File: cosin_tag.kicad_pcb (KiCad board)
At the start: 2 copper layers, 81 x 34 mm, 65 parts, among them IC1 ATTINY13-SS, P1 ISP, Q1 2N7002, Q2 2N7002, Q3 2N7002, Q4 2N7002, Q5 2N7002

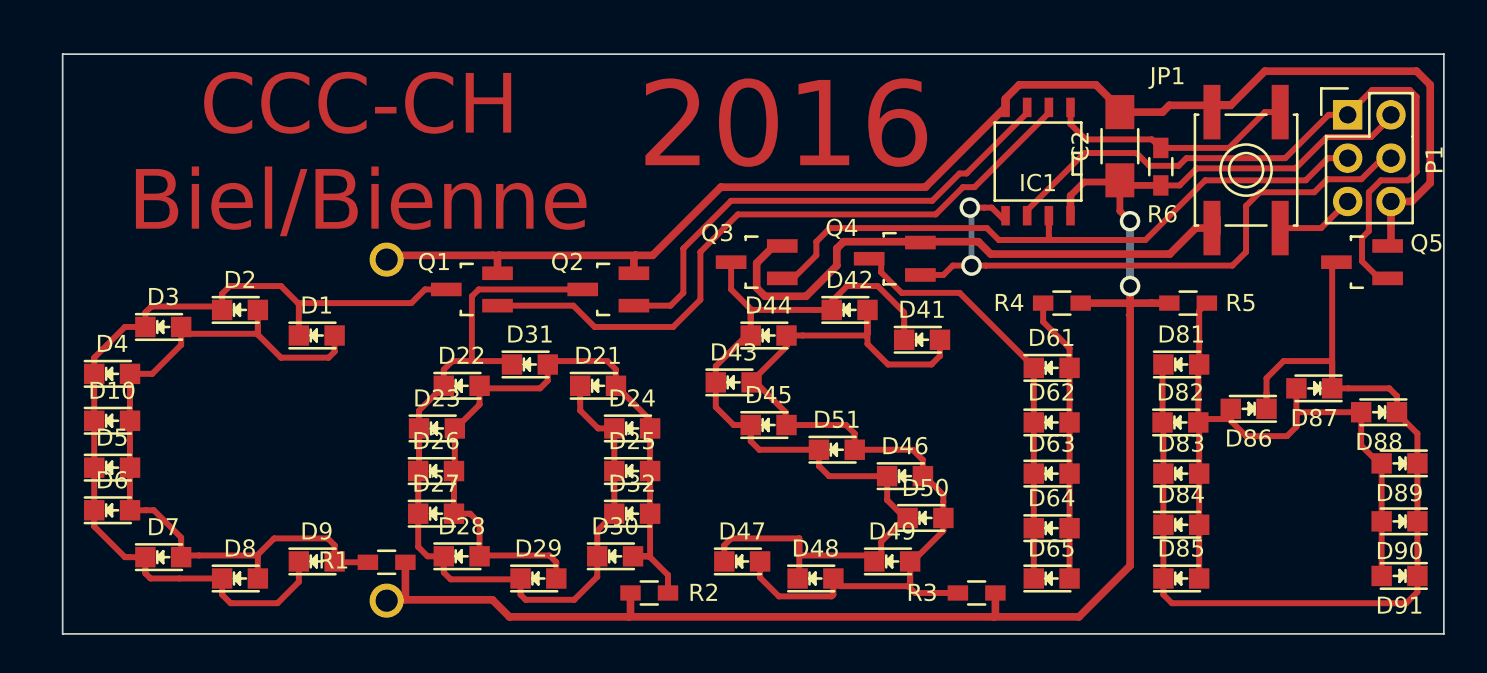
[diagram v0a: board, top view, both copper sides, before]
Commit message: Minimized the areas in the layout where the tracks are close together. Made the tracks around the microcontroller smaller to improve yield when etching the PCB at home. For this a new netclass was introduced and the global cleareance rule is now higher. Cleaned up the values and references on the board and added a output PDF to show the placing of the components.
Added the resistor values to the schematic.

Updated all output files.
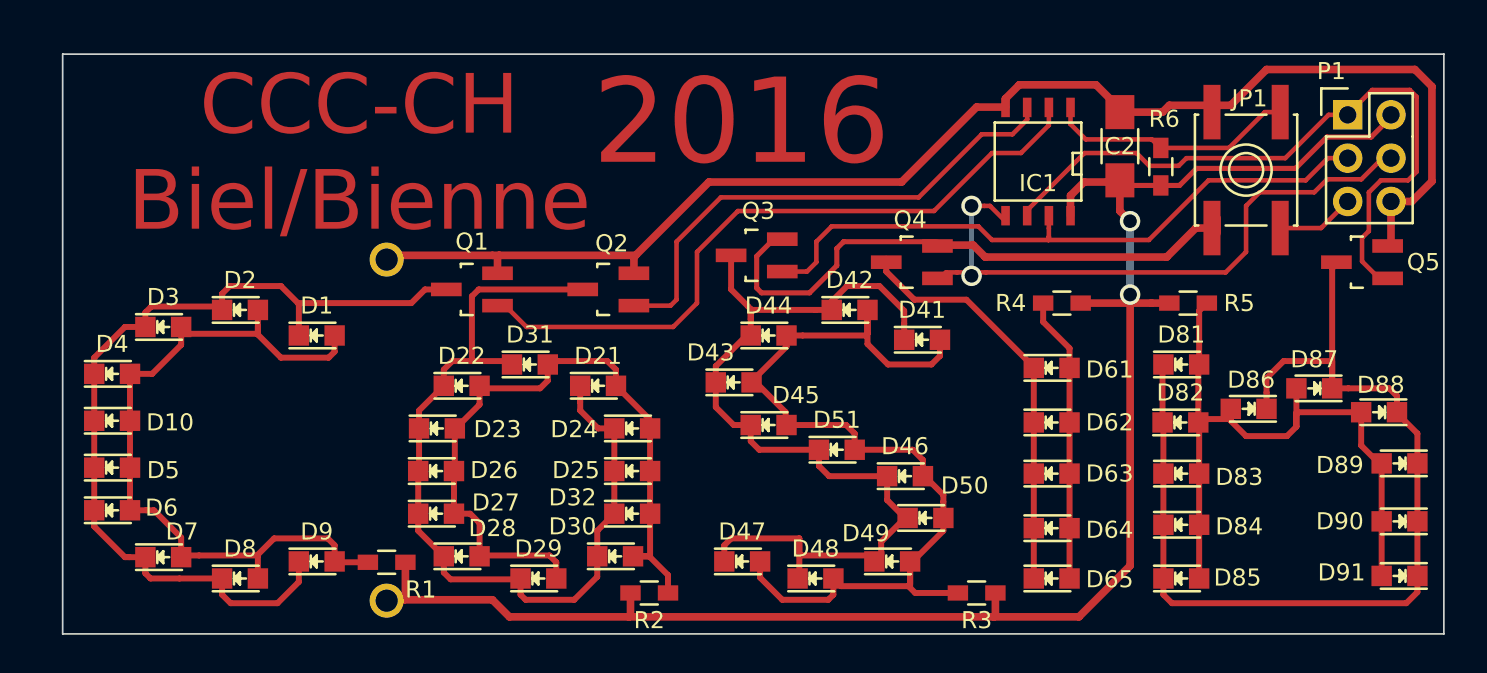
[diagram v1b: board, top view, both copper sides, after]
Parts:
- R1, R3, R5: value 0 -> 10
- R2: value 0 -> 8.2
- R4: value 0 -> 24
- moved Q4 1.02 mm to (169.6, 71.2)
- moved Q3 0.40 mm to (160.5, 70.8)
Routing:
- net Net-(D61-Pad1): track 25.2 -> 24.1 mm
- net /DIGIT1: track 29.6 -> 30.3 mm
- net /DIGIT3: track 38.1 -> 37.5 mm
- net GND: track 116.3 -> 116.9 mm
- net Net-(D21-Pad1): track 52.3 -> 51.7 mm
- net /DIGIT0: track 40.0 -> 40.6 mm
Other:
- net class Default: trace_width 0.35 -> 0.27
- net class Led added: clearance 0.4, trace_width 0.35, via_dia 1.2, via_drill 0.8
- rule trace_min: 0.35 -> 0.25
